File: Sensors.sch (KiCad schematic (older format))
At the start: 17 parts, among them IC2 MAX11128ATI+, IC3 MAX11128ATI+, J6 Conn_01x04_Female, Q2 BSS138, Q3 BSS138, U2 REF3030

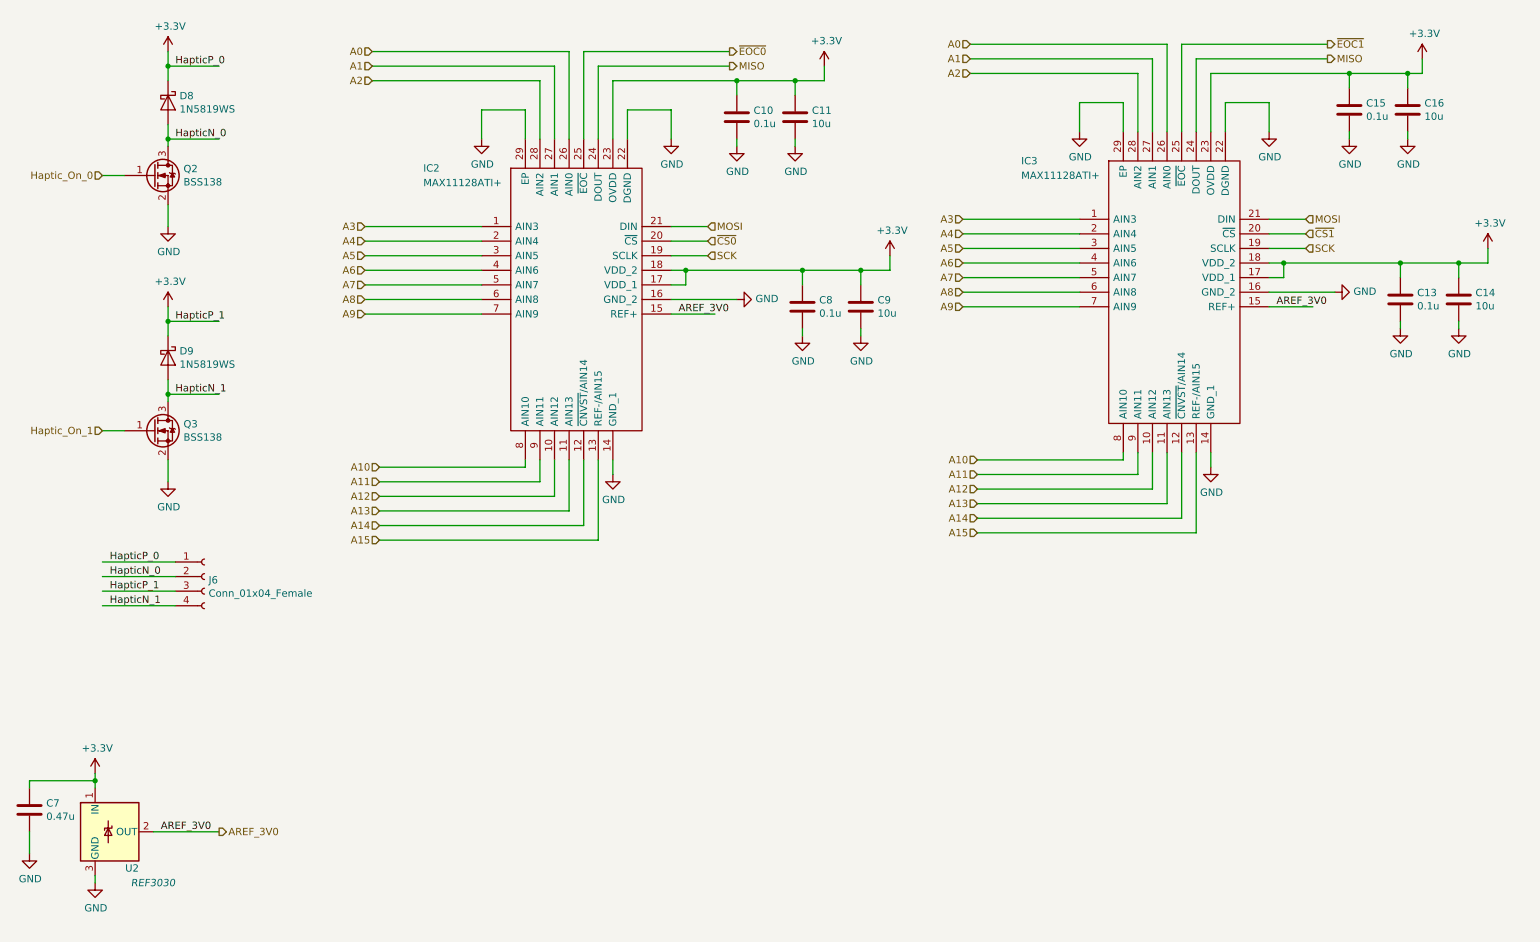
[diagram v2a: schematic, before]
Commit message: Changed to 4-layer board, added power shapes in layout.
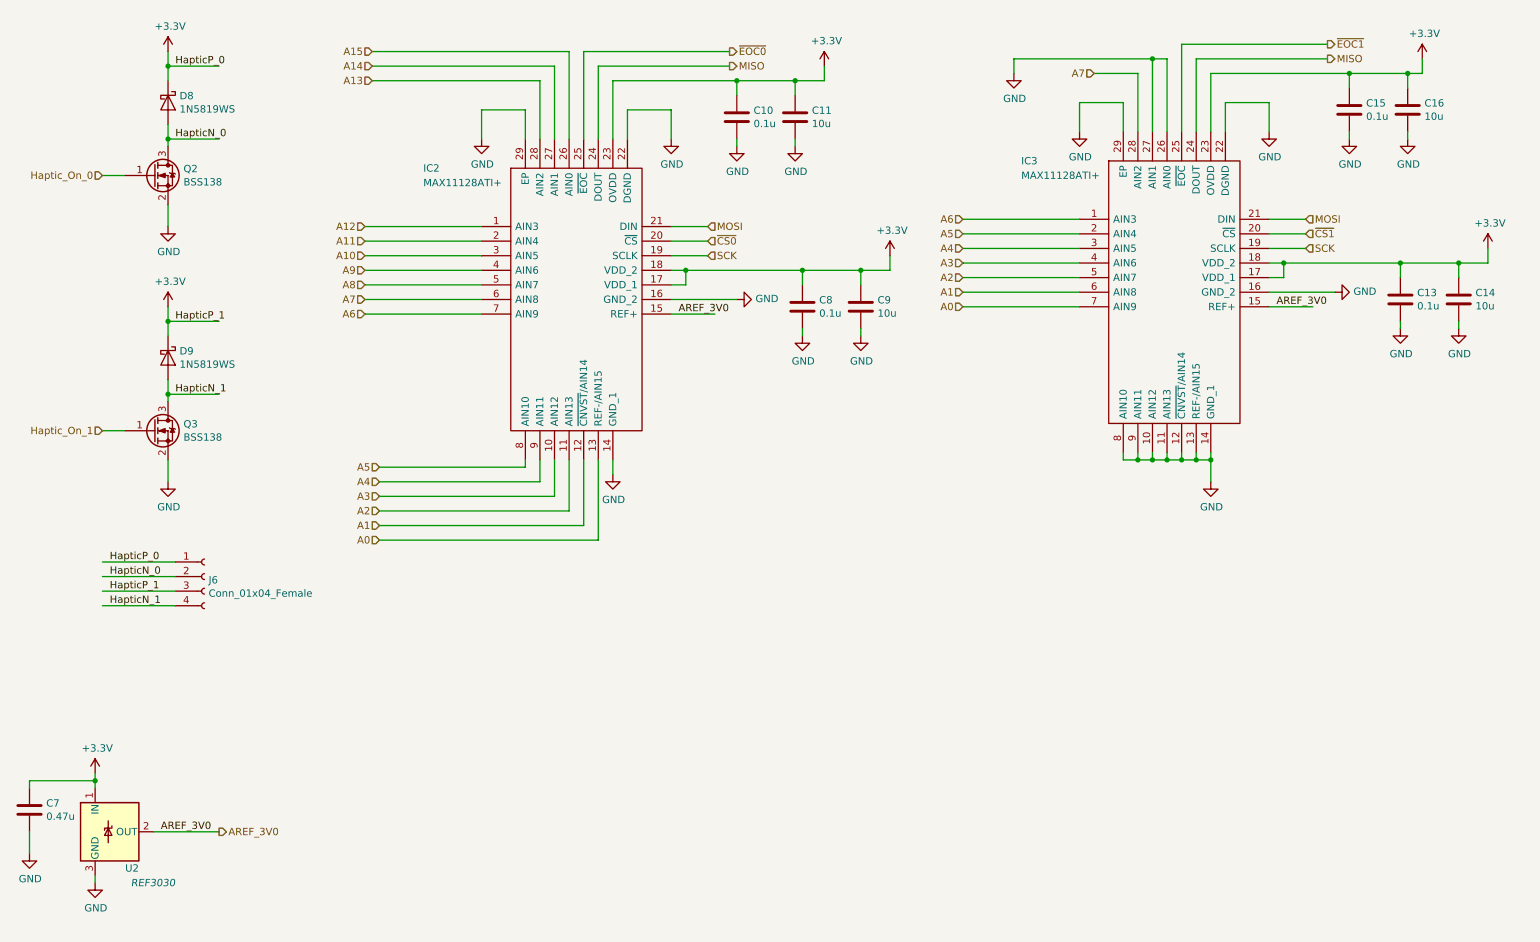
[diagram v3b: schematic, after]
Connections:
- wire segments 149 -> 151
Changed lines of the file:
@@
 $EndComp
-Wire Wire Line
-	3900 2650 3100 2650
-Wire Wire Line
-	3900 3050 3100 3050
-Wire Wire Line
-	3900 2950 3100 2950
-Wire Wire Line
-	3900 2850 3100 2850
-Wire Wire Line
-	3900 2750 3100 2750
 Wire Wire Line
 	4200 2050 4200 1850
@@
 	6700 2950 6700 2850
 Text HLabel 3150 1450 0    50   Input ~ 0
-A0
+A15
 Text HLabel 3150 1550 0    50   Input ~ 0
-A1
+A14
 Text HLabel 3150 1650 0    50   Input ~ 0
-A2
-Text HLabel 3100 2650 0    50   Input ~ 0
-A3
-Text HLabel 3100 2750 0    50   Input ~ 0
-A4
-Text HLabel 3100 2850 0    50   Input ~ 0
-A5
-Text HLabel 3100 2950 0    50   Input ~ 0
-A6
-Text HLabel 3100 3050 0    50   Input ~ 0
-A7
-Text HLabel 3100 3150 0    50   Input ~ 0
-A8
-Text HLabel 3100 3250 0    50   Input ~ 0
-A9
-Text HLabel 3200 4300 0    50   Input ~ 0
-A10
-Text HLabel 3200 4400 0    50   Input ~ 0
-A11
-Text HLabel 3200 4500 0    50   Input ~ 0
-A12
-Text HLabel 3200 4600 0    50   Input ~ 0
 A13
-Text HLabel 3200 4700 0    50   Input ~ 0
-A14
-Text HLabel 3200 4800 0    50   Input ~ 0
-A15
 $Comp
 L Reference_Voltage:REF3030 U2
@@
 	8300 4200 8300 4250
 Wire Wire Line
-	8800 4750 8800 4200
-Wire Wire Line
-	8700 4200 8700 4650
-Wire Wire Line
-	8600 4200 8600 4550
-Wire Wire Line
-	8500 4200 8500 4450
-Wire Wire Line
-	8400 4200 8400 4350
-Wire Wire Line
 	8400 2000 8400 1600
 Wire Wire Line
-	8400 1600 7250 1600
+	8400 1600 8100 1600
 Wire Wire Line
 	8500 2000 8500 1500
 Wire Wire Line
-	8500 1500 7250 1500
-Wire Wire Line
-	8600 2000 8600 1400
-Wire Wire Line
-	8600 1400 7250 1400
+	8600 2000 8600 1500
 Wire Wire Line
 	9750 3100 9300 3100
@@
 L power:GND #PWR060
 U 1 1 5FC6D472
-P 8900 4300
-F 0 "#PWR060" H 8900 4050 50  0001 C CNN
-F 1 "GND" H 8905 4127 50  0000 C CNN
-F 2 "" H 8900 4300 50  0001 C CNN
-F 3 "" H 8900 4300 50  0001 C CNN
-	1    8900 4300
-	1    0    0    -1
-$EndComp
-Wire Wire Line
-	8900 4200 8900 4300
+P 8900 4400
+F 0 "#PWR060" H 8900 4150 50  0001 C CNN
+F 1 "GND" H 8905 4227 50  0000 C CNN
+F 2 "" H 8900 4400 50  0001 C CNN
+F 3 "" H 8900 4400 50  0001 C CNN
+	1    8900 4400
+	1    0    0    -1
+$EndComp
 $Comp
 L Device:C C10
@@
 Wire Wire Line
 	10800 2900 10800 2800
-Text HLabel 7250 1400 0    50   Input ~ 0
+Text HLabel 8100 1600 0    50   Input ~ 0
+A7
+Text HLabel 7200 2600 0    50   Input ~ 0
+A6
+Text HLabel 7200 2700 0    50   Input ~ 0
+A5
+Text HLabel 7200 2800 0    50   Input ~ 0
+A4
+Text HLabel 7200 2900 0    50   Input ~ 0
+A3
+Text HLabel 7200 3000 0    50   Input ~ 0
+A2
+Text HLabel 7200 3100 0    50   Input ~ 0
+A1
+Text HLabel 7200 3200 0    50   Input ~ 0
 A0
-Text HLabel 7250 1500 0    50   Input ~ 0
-A1
-Text HLabel 7250 1600 0    50   Input ~ 0
-A2
-Text HLabel 7200 2600 0    50   Input ~ 0
-A3
-Text HLabel 7200 2700 0    50   Input ~ 0
-A4
-Text HLabel 7200 2800 0    50   Input ~ 0
-A5
-Text HLabel 7200 2900 0    50   Input ~ 0
-A6
-Text HLabel 7200 3000 0    50   Input ~ 0
-A7
-Text HLabel 7200 3100 0    50   Input ~ 0
-A8
-Text HLabel 7200 3200 0    50   Input ~ 0
-A9
-Text HLabel 7300 4250 0    50   Input ~ 0
-A10
-Text HLabel 7300 4350 0    50   Input ~ 0
-A11
-Text HLabel 7300 4450 0    50   Input ~ 0
-A12
-Text HLabel 7300 4550 0    50   Input ~ 0
-A13
-Text HLabel 7300 4650 0    50   Input ~ 0
-A14
-Text HLabel 7300 4750 0    50   Input ~ 0
-A15
 Wire Wire Line
 	9300 3200 9600 3200
@@
 	1650 6800 2100 6800
 Wire Wire Line
-	3200 4300 4200 4300
-Wire Wire Line
-	3200 4400 4300 4400
-Wire Wire Line
-	3200 4500 4400 4500
-Wire Wire Line
-	3200 4600 4500 4600
-Wire Wire Line
-	3200 4700 4600 4700
-Wire Wire Line
-	3200 4800 4700 4800
-Wire Wire Line
-	7300 4250 8300 4250
-Wire Wire Line
-	7300 4350 8400 4350
-Wire Wire Line
-	7300 4450 8500 4450
-Wire Wire Line
-	7300 4550 8600 4550
-Wire Wire Line
-	7300 4650 8700 4650
-Wire Wire Line
-	7300 4750 8800 4750
-Wire Wire Line
 	7200 3100 8000 3100
 Wire Wire Line
 	7200 3200 8000 3200
-Wire Wire Line
-	3100 3150 3900 3150
-Wire Wire Line
-	3100 3250 3900 3250
 $Comp
 L Device:C C15
@@
 	1    0    0    -1
 $EndComp
+Wire Wire Line
+	3100 3250 3900 3250
+Wire Wire Line
+	3100 3150 3900 3150
+Wire Wire Line
+	3200 4800 4700 4800
+Wire Wire Line
+	3200 4700 4600 4700
+Wire Wire Line
+	3200 4600 4500 4600
+Wire Wire Line
+	3200 4500 4400 4500
+Wire Wire Line
+	3200 4400 4300 4400
+Wire Wire Line
+	3200 4300 4200 4300
+Text HLabel 3200 4800 0    50   Input ~ 0
+A0
+Text HLabel 3200 4700 0    50   Input ~ 0
+A1
+Text HLabel 3200 4600 0    50   Input ~ 0
+A2
+Text HLabel 3200 4500 0    50   Input ~ 0
+A3
+Text HLabel 3200 4400 0    50   Input ~ 0
+A4
+Text HLabel 3200 4300 0    50   Input ~ 0
+A5
+Text HLabel 3100 3250 0    50   Input ~ 0
+A6
+Text HLabel 3100 3150 0    50   Input ~ 0
+A7
+Text HLabel 3100 2950 0    50   Input ~ 0
+A9
+Text HLabel 3100 2850 0    50   Input ~ 0
+A10
+Text HLabel 3100 2750 0    50   Input ~ 0
+A11
+Text HLabel 3100 2650 0    50   Input ~ 0
+A12
+Wire Wire Line
+	3900 2750 3100 2750
+Wire Wire Line
+	3900 2850 3100 2850
+Wire Wire Line
+	3900 2950 3100 2950
+Wire Wire Line
+	3900 3050 3100 3050
+Wire Wire Line
+	3900 2650 3100 2650
+Text HLabel 3100 3050 0    50   Input ~ 0
+A8
+Wire Wire Line
+	8900 4200 8900 4250
+Wire Wire Line
+	8300 4250 8400 4250
+Connection ~ 8900 4250
+Wire Wire Line
+	8900 4250 8900 4400
+Wire Wire Line
+	8400 4200 8400 4250
+Connection ~ 8400 4250
+Wire Wire Line
+	8400 4250 8500 4250
+Wire Wire Line
+	8500 4200 8500 4250
+Connection ~ 8500 4250
+Wire Wire Line
+	8500 4250 8600 4250
+Wire Wire Line
+	8600 4200 8600 4250
+Connection ~ 8600 4250
+Wire Wire Line
+	8600 4250 8700 4250
+Wire Wire Line
+	8700 4200 8700 4250
+Connection ~ 8700 4250
+Wire Wire Line
+	8700 4250 8800 4250
+Wire Wire Line
+	8800 4200 8800 4250
+Connection ~ 8800 4250
+Wire Wire Line
+	8800 4250 8900 4250
+$Comp
+L power:GND #PWR0102
+U 1 1 5FD2D6C9
+P 7550 1600
+F 0 "#PWR0102" H 7550 1350 50  0001 C CNN
+F 1 "GND" H 7555 1427 50  0000 C CNN
+F 2 "" H 7550 1600 50  0001 C CNN
+F 3 "" H 7550 1600 50  0001 C CNN
+	1    7550 1600
+	1    0    0    -1
+$EndComp
+Wire Wire Line
+	8500 1500 7550 1500
+Wire Wire Line
+	7550 1500 7550 1600
+Wire Wire Line
+	8500 1500 8600 1500
+Connection ~ 8500 1500
 $EndSCHEMATC

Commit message: Added high side R for sensors and buck-boost. Replaced 3.0V VRef with LDO. BOM rev 1. Finished layout. TODO: Silkscreen.
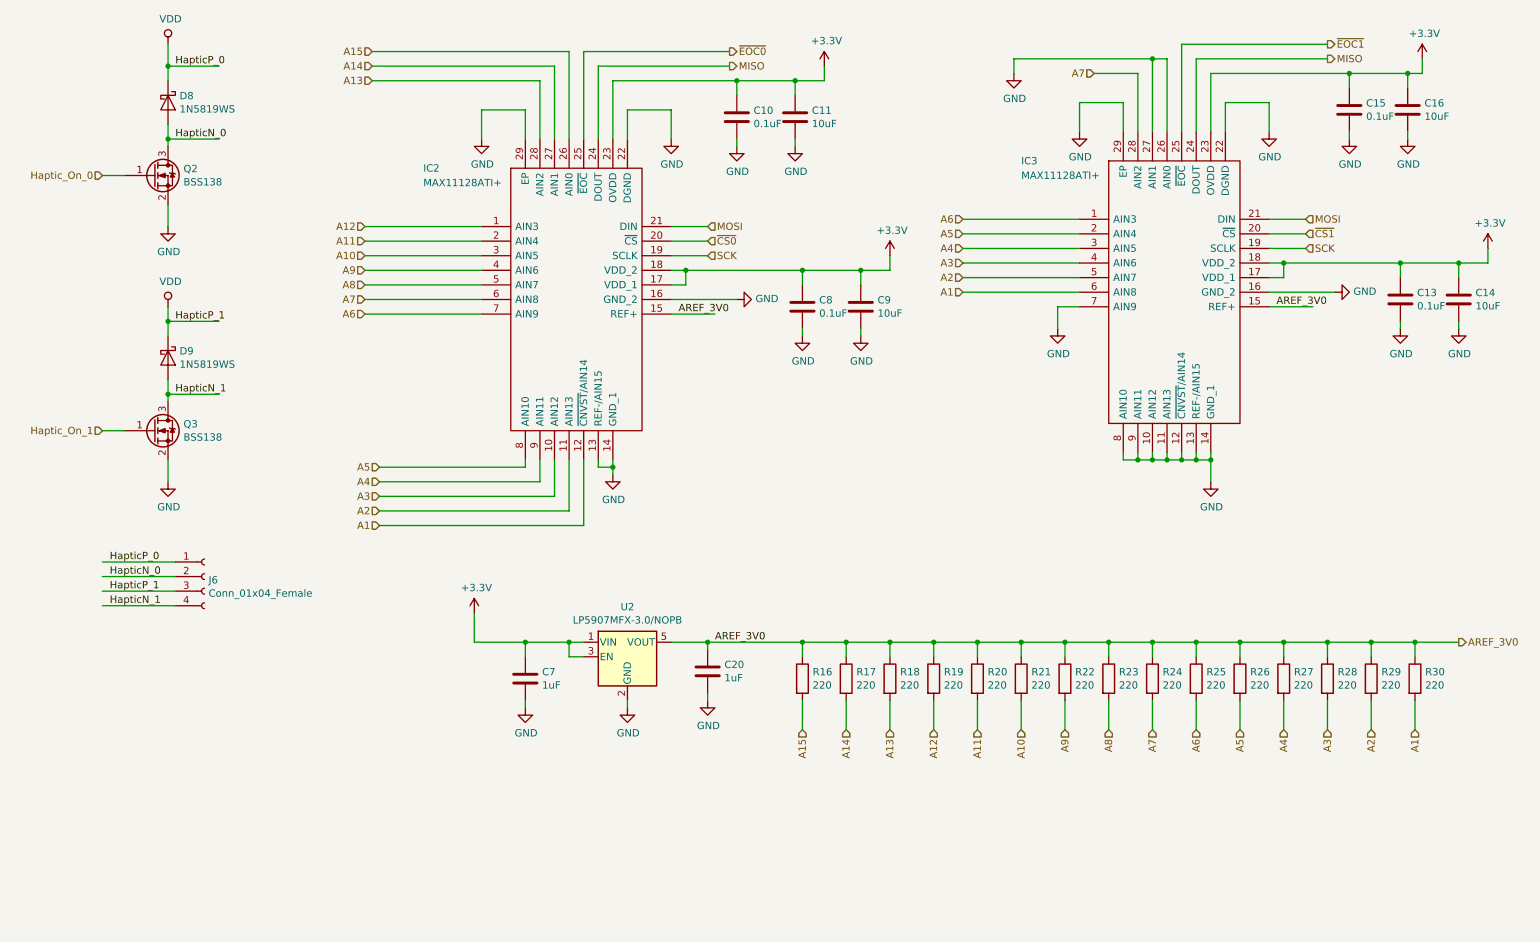
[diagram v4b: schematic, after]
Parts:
- removed U2: REF3030, Package_TO_SOT_SMD:SOT-23, symbol Reference_Voltage:REF3030
- added C20: 1uF, Capacitors_SMD:C_0603_HandSoldering, symbol Device:C
- added R16, R17, R18, R19, R20, R21, R22, R23, R24, R25, R26, R27, R28, R29, R30: 220, Resistors_SMD:R_0603_HandSoldering, symbol Device:R
- added U2: LP5907MFX-3.0/NOPB, Package_TO_SOT_SMD:SOT-23-5, symbol Regulator_Linear:AP2112K-3.3
- C10, C13, C15, C8: value 0.1u -> 0.1uF; Description (none) -> MULTILAYER CERAMIC CAPACITORS MLCC - SMD/SMT 100NF 50V 0603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; LCSC (none) -> C14663; MPN (none) -> CC0603KRX7R9BB104; Manufacturer (none) -> YAGEO
- C11, C14, C16, C9: value 10u -> 10uF; Description (none) -> MULTILAYER CERAMIC CAPACITORS MLCC - SMD/SMT 10UF 10V 0603 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; LCSC (none) -> C19702; MPN (none) -> CL10A106KP8NNNC; Manufacturer (none) -> Samsung Electro-Mechanics
- C7: value 0.47u -> 1uF; Description (none) -> MULTILAYER CERAMIC CAPACITORS MLCC - SMD/SMT 1UF 50V 0603 R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; LCSC (none) -> C15849; MPN (none) -> CL10A105KB8NNNC; Manufacturer (none) -> Samsung Electro-Mechanics
- D8, D9: Description (none) -> SCHOTTKY BARRIER DIODES (SBD) SOD-323 ROHS; LCSC (none) -> C191023; MPN (none) -> 1N5819WS; Manufacturer (none) -> Guangdong Hottech
- IC2, IC3: LCSC (none) -> -; MPN (none) -> -; Manufacturer (none) -> -
- J6: Description (none) -> -; LCSC (none) -> -; MPN (none) -> -; Manufacturer (none) -> -
- Q2, Q3: Description (none) -> MOSFET N TRENCH 50V 220MA 1.5V @ 1MA 3.5 ? @ 220MA,10V SOT-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; LCSC (none) -> C52895; MPN (none) -> BSS138; Manufacturer (none) -> ON Semicon
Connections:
- net labels added: VDD
- net labels removed: A0
- wire segments 151 -> 204
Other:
- moved on the sheet: C7
